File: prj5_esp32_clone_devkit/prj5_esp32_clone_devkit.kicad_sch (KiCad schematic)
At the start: 0 parts

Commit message: Inserimento componenti
Feat: inseriti i simboli dei componenti
Feat: annotati i simboli in modo coerente allo schema di ESP32
Feat: sistemati i posizionamenti
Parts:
- added C1, C21, C3: 22uF/10V(20%), symbol Device:C
- added C14, C22, C9: 0.1uF/50V(10%), symbol Device:C
- added C15: 0.1uF/50V(10%)(NC), symbol Device:C
- added C19: 0.1uf/50V(10%), symbol Device:C
- added C20: 4.7uf/6.3V(10%), symbol Device:C
- added D1: LED, symbol Device:LED
- added D3: D_Schottky, symbol Device:D_Schottky
- added D4, D5, D6: D_TVS, symbol Device:D_TVS
- added J1: USB_B_Micro, symbol Connector:USB_B_Micro
- added J2, J3: Conn_01x19_Pin, symbol Connector:Conn_01x19_Pin
- added MOD1: ESP32-WROOM-32, digikey-footprints:ESP32-WROOM-32D, symbol dk_RF-Transceiver-Modules:ESP32-WROOM-32
- added Q1, Q2: MMSS8050-H-TP, digikey-footprints:SOT-23-3, symbol dk_Transistors-Bipolar-BJT-Single:MMSS8050-H-TP
- added R11, R21, R22: 10K(5%), symbol Device:R
- added R17, R18: 0R(5%), symbol Device:R
- added R2, R24: 2K(5%), symbol Device:R
- added R23: 10K(5%)(NC), symbol Device:R
- added R25: 22.1K(5%), symbol Device:R
- added R28: 47.5K(5%), symbol Device:R
- added SW1, SW2: SW_Push, symbol Switch:SW_Push
- added U1: CP2102N-A01-GQFN28, QFN50P500X500X80-29N, symbol CP2102N-A01-GQFN28:CP2102N-A01-GQFN28
- added U2: AMS1117-3.3, Package_TO_SOT_SMD:SOT-223-3_TabPin2, symbol Regulator_Linear:AMS1117-3.3
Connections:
- new net: U1.29 (GND), U1.3 (GND)
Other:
- note added: "Connector"
- note added: "ESP32 Module"
- note added: "Micro USB 5V & USB-UART"
- note added: "Power Supply"
- note added: "Switch button"

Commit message: Associazione footprint
Feat: associati i footprint ai simboli dello schematico (coerentemente con la BOM)
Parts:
- C1, C21, C3: footprint (none) -> Capacitor_SMD:C_0603_1608Metric
- C14, C15, C19, C20, C22, C9: footprint (none) -> Capacitor_SMD:C_0402_1005Metric
- D1: footprint (none) -> LED_SMD:LED_0603_1608Metric
- D3: footprint (none) -> Diode_SMD:D_SOD-323
- D4, D5, D6: footprint (none) -> Diode_SMD:D_SOD-523
- J1: footprint (none) -> Connector_USB:USB_Micro-AB_Molex_47590-0001
- J2, J3: footprint (none) -> Connector_PinHeader_2.54mm:PinHeader_1x19_P2.54mm_Vertical
- R11, R17, R18, R2, R21, R22, R23, R24, R25, R28: footprint (none) -> Resistor_SMD:R_01005_0402Metric
- SW1, SW2: footprint (none) -> Button_Switch_SMD:SW_SPST_B3S-1000
- U1: footprint QFN50P500X500X80-29N -> Package_DFN_QFN:TQFN-28-1EP_5x5mm_P0.5mm_EP2.7x2.7mm
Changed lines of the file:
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@@
       (effects (font (size 1.27 1.27)))
     )
-    (property "Footprint" "" (at 30.48 98.298 90)
+    (property "Footprint" "Resistor_SMD:R_01005_0402Metric" (at 30.48 98.298 90)
       (effects (font (size 1.27 1.27)) hide)
     )
@@
       (effects (font (size 1.27 1.27)))
     )
-    (property "Footprint" "" (at 38.1 81.788 90)
+    (property "Footprint" "Resistor_SMD:R_01005_0402Metric" (at 38.1 81.788 90)
       (effects (font (size 1.27 1.27)) hide)
     )
@@
       (effects (font (size 1.27 1.27)) (justify left))
     )
-    (property "Footprint" "" (at 144.4752 31.75 0)
+    (property "Footprint" "Capacitor_SMD:C_0402_1005Metric" (at 144.4752 31.75 0)
       (effects (font (size 1.27 1.27)) hide)
     )
@@
       (effects (font (size 1.27 1.27)))
     )
-    (property "Footprint" "" (at 29.21 31.75 0)
+    (property "Footprint" "Connector_USB:USB_Micro-AB_Molex_47590-0001" (at 29.21 31.75 0)
       (effects (font (size 1.27 1.27)) hide)
     )
@@
       (effects (font (size 1.27 1.27)) (justify left))
     )
-    (property "Footprint" "" (at 139.192 46.99 90)
+    (property "Footprint" "Resistor_SMD:R_01005_0402Metric" (at 139.192 46.99 90)
       (effects (font (size 1.27 1.27)) hide)
     )
@@
       (effects (font (size 1.27 1.27)) (justify left))
     )
-    (property "Footprint" "" (at 28.702 153.67 90)
+    (property "Footprint" "Resistor_SMD:R_01005_0402Metric" (at 28.702 153.67 90)
       (effects (font (size 1.27 1.27)) hide)
     )
@@
       (effects (font (size 1.27 1.27)) (justify right))
     )
-    (property "Footprint" "" (at 30.48 165.1 0)
+    (property "Footprint" "LED_SMD:LED_0603_1608Metric" (at 30.48 165.1 0)
       (effects (font (size 1.27 1.27)) hide)
     )
@@
       (effects (font (size 1.27 1.27)) (justify left))
     )
-    (property "Footprint" "" (at 189.992 54.61 90)
+    (property "Footprint" "Resistor_SMD:R_01005_0402Metric" (at 189.992 54.61 90)
       (effects (font (size 1.27 1.27)) hide)
     )
@@
       (effects (font (size 1.27 1.27)) (justify left))
     )
-    (property "Footprint" "" (at 45.4152 162.56 0)
+    (property "Footprint" "Capacitor_SMD:C_0603_1608Metric" (at 45.4152 162.56 0)
       (effects (font (size 1.27 1.27)) hide)
     )
@@
       (effects (font (size 1.27 1.27)))
     )
-    (property "Footprint" "" (at 29.21 113.538 90)
+    (property "Footprint" "Resistor_SMD:R_01005_0402Metric" (at 29.21 113.538 90)
       (effects (font (size 1.27 1.27)) hide)
     )
@@
       (effects (font (size 1.27 1.27)))
     )
-    (property "Footprint" "" (at 73.66 76.708 90)
+    (property "Footprint" "Resistor_SMD:R_01005_0402Metric" (at 73.66 76.708 90)
       (effects (font (size 1.27 1.27)) hide)
     )
@@
       (effects (font (size 1.27 1.27)) (justify left))
     )
-    (property "Footprint" "" (at 192.7352 40.64 0)
+    (property "Footprint" "Capacitor_SMD:C_0603_1608Metric" (at 192.7352 40.64 0)
       (effects (font (size 1.27 1.27)) hide)
     )
@@
       (effects (font (size 1.27 1.27)) (justify left))
     )
-    (property "Footprint" "" (at 192.7352 71.12 0)
+    (property "Footprint" "Capacitor_SMD:C_0402_1005Metric" (at 192.7352 71.12 0)
       (effects (font (size 1.27 1.27)) hide)
     )
@@
       (effects (font (size 1.27 1.27)) (justify right))
     )
-    (property "Footprint" "" (at 58.42 39.37 0)
+    (property "Footprint" "Diode_SMD:D_SOD-523" (at 58.42 39.37 0)
       (effects (font (size 1.27 1.27)) hide)
     )
@@
       (effects (font (size 1.27 1.27)))
     )
-    (property "Footprint" "" (at 38.1 71.628 90)
+    (property "Footprint" "Resistor_SMD:R_01005_0402Metric" (at 38.1 71.628 90)
       (effects (font (size 1.27 1.27)) hide)
     )
@@
       (effects (font (size 1.27 1.27)))
     )
-    (property "Footprint" "" (at 147.32 40.513 90)
+    (property "Footprint" "Resistor_SMD:R_01005_0402Metric" (at 147.32 40.513 90)
       (effects (font (size 1.27 1.27)) hide)
     )
@@
       (effects (font (size 1.27 1.27)))
     )
-    (property "Footprint" "" (at 227.33 132.08 0)
+    (property "Footprint" "Connector_PinHeader_2.54mm:PinHeader_1x19_P2.54mm_Vertical" (at 227.33 132.08 0)
       (effects (font (size 1.27 1.27)) hide)
     )
@@
       (effects (font (size 1.27 1.27)) (justify right))
     )
-    (property "Footprint" "" (at 38.1 39.37 0)
+    (property "Footprint" "Diode_SMD:D_SOD-523" (at 38.1 39.37 0)
       (effects (font (size 1.27 1.27)) hide)
     )
@@
       (effects (font (size 1.27 1.27)) (justify left))
     )
-    (property "Footprint" "" (at 78.4352 162.56 0)
+    (property "Footprint" "Capacitor_SMD:C_0603_1608Metric" (at 78.4352 162.56 0)
       (effects (font (size 1.27 1.27)) hide)
     )
@@
       (effects (font (size 1.27 1.27)))
     )
-    (property "Footprint" "" (at 265.43 132.08 0)
+    (property "Footprint" "Connector_PinHeader_2.54mm:PinHeader_1x19_P2.54mm_Vertical" (at 265.43 132.08 0)
       (effects (font (size 1.27 1.27)) hide)
     )
@@
       (effects (font (size 1.27 1.27)) (justify right))
     )
-    (property "Footprint" "" (at 48.26 39.37 0)
+    (property "Footprint" "Diode_SMD:D_SOD-523" (at 48.26 39.37 0)
       (effects (font (size 1.27 1.27)) hide)
     )
@@
       (effects (font (size 1.27 1.27)) (justify left))
     )
-    (property "Footprint" "" (at 209.2452 40.64 0)
+    (property "Footprint" "Capacitor_SMD:C_0402_1005Metric" (at 209.2452 40.64 0)
       (effects (font (size 1.27 1.27)) hide)
     )
@@
       (effects (font (size 1.27 1.27)))
     )
-    (property "Footprint" "QFN50P500X500X80-29N" (at 106.68 64.77 0)
+    (property "Footprint" "Package_DFN_QFN:TQFN-28-1EP_5x5mm_P0.5mm_EP2.7x2.7mm" (at 106.68 64.77 0)
       (effects (font (size 1.27 1.27)) (justify bottom) hide)
     )
@@
       (effects (font (size 1.27 1.27)))
     )
-    (property "Footprint" "" (at 128.27 164.1348 0)
+    (property "Footprint" "Capacitor_SMD:C_0402_1005Metric" (at 128.27 164.1348 0)
       (effects (font (size 1.27 1.27)) hide)
     )
@@
       (effects (font (size 1.27 1.27)))
     )
-    (property "Footprint" "" (at 152.4 147.32 0)
+    (property "Footprint" "Button_Switch_SMD:SW_SPST_B3S-1000" (at 152.4 147.32 0)
       (effects (font (size 1.27 1.27)) hide)
     )
@@
       (effects (font (size 1.27 1.27)))
     )
-    (property "Footprint" "" (at 156.21 164.1348 0)
+    (property "Footprint" "Capacitor_SMD:C_0402_1005Metric" (at 156.21 164.1348 0)
       (effects (font (size 1.27 1.27)) hide)
     )
@@
       (effects (font (size 1.27 1.27)) (justify left))
     )
-    (property "Footprint" "" (at 149.352 78.74 90)
+    (property "Footprint" "Resistor_SMD:R_01005_0402Metric" (at 149.352 78.74 90)
       (effects (font (size 1.27 1.27)) hide)
     )
@@
       (effects (font (size 1.27 1.27)) (justify left))
     )
-    (property "Footprint" "" (at 158.4452 31.75 0)
+    (property "Footprint" "Capacitor_SMD:C_0402_1005Metric" (at 158.4452 31.75 0)
       (effects (font (size 1.27 1.27)) hide)
     )
@@
       (effects (font (size 1.27 1.27)))
     )
-    (property "Footprint" "" (at 64.77 25.4 0)
+    (property "Footprint" "Diode_SMD:D_SOD-323" (at 64.77 25.4 0)
       (effects (font (size 1.27 1.27)) hide)
     )
@@
       (effects (font (size 1.27 1.27)))
     )
-    (property "Footprint" "" (at 124.46 147.32 0)
-      (effects (font (size 1.27 1.27)) hide)
-    )
+    (property "Footprint" "Button_Switch_SMD:SW_SPST_B3S-1000" (at 124.46 147.32 0)
+      (effects (font (size 1.27 1.27)) hide)
+    )

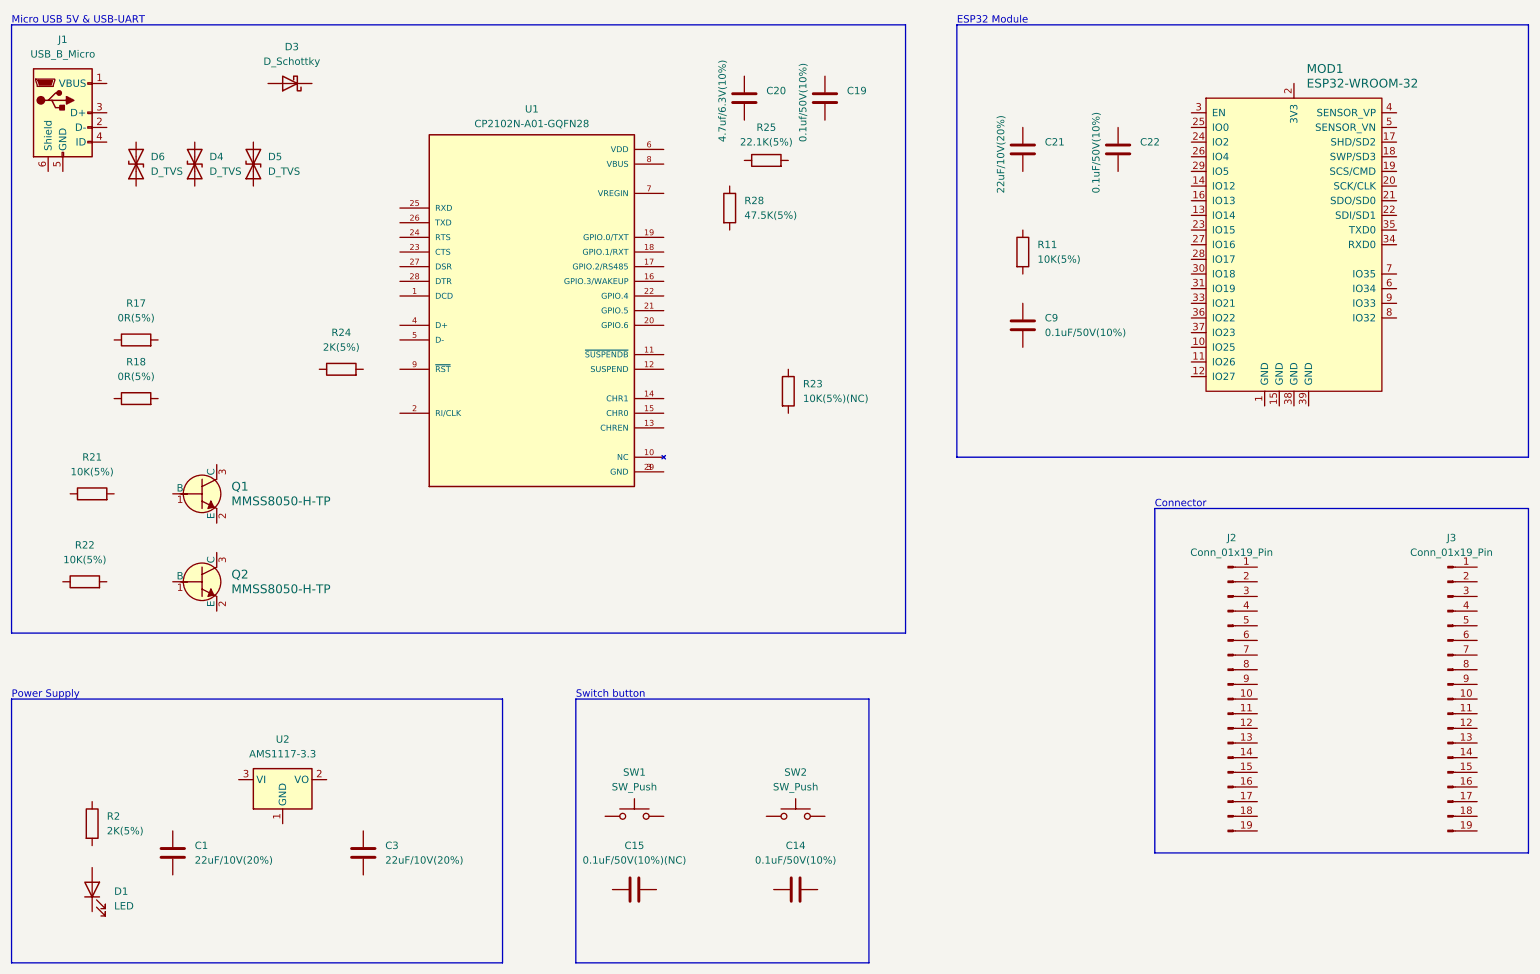
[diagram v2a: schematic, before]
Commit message: Connessioni componenti schematico
Feat: concluso il wiring dei simboli
Feat: aggiustati alcuni posizionamenti
Feat: aggiunto commento con tabella di verità
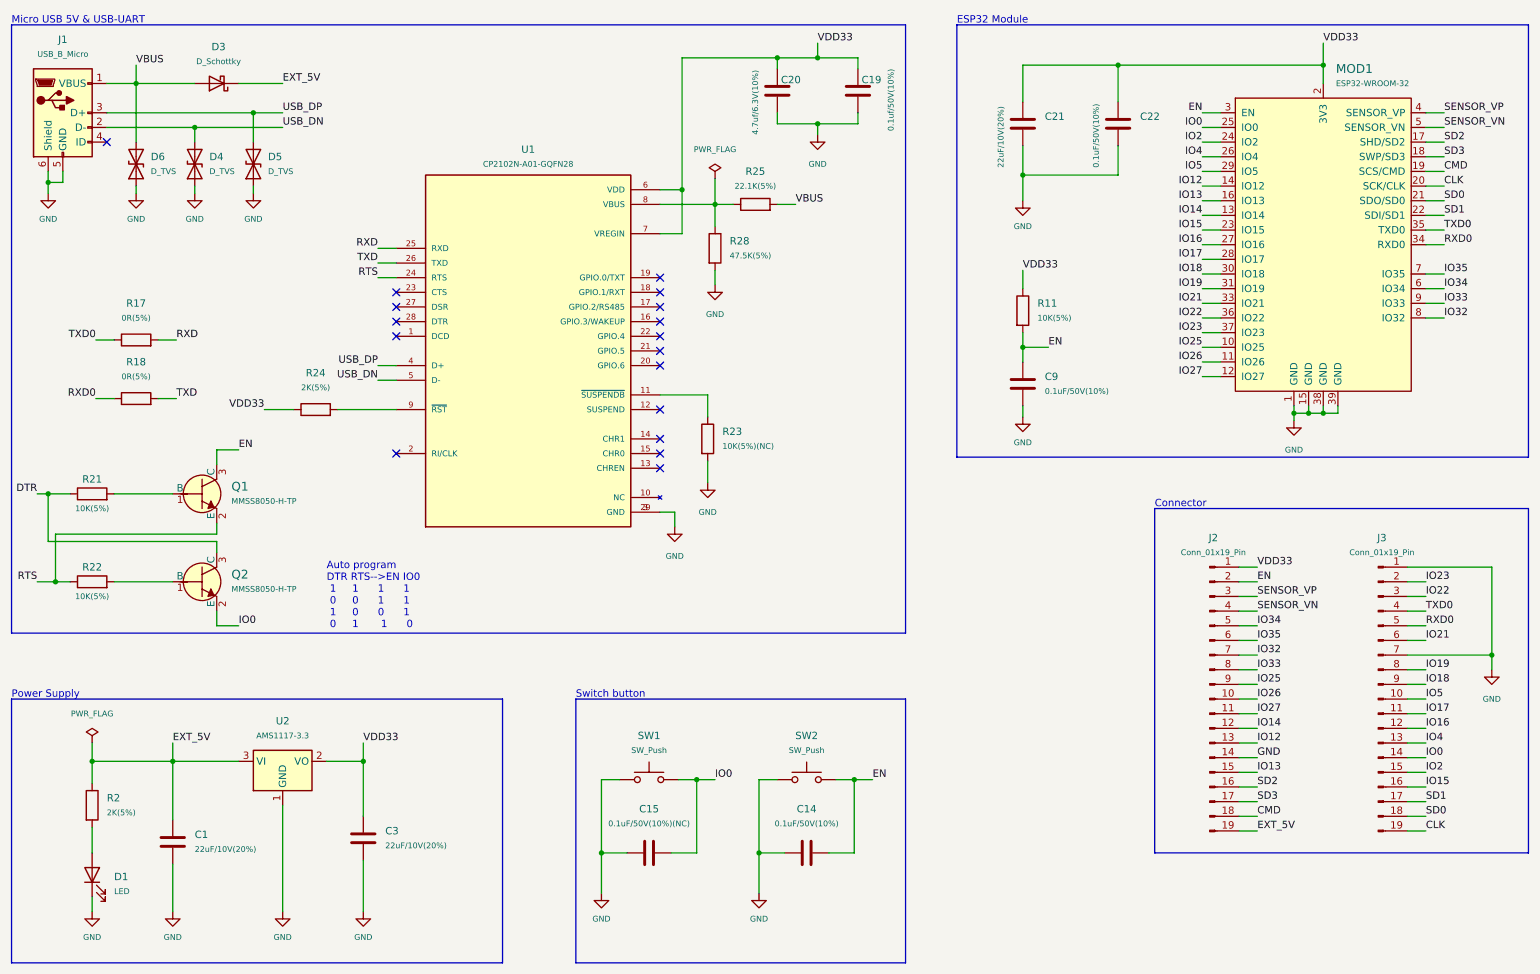
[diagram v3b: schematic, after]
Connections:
- net DTR: now reaches R21.1
- net DTR: now also Q2.3 (C)
- net at R21.2: now also Q1.1 (B)
- net RXD0: now reaches R18.1
- net RXD0: now also J3.5 (Pin_5), MOD1.34 (RXD0)
- net TXD: now reaches R18.2
- net TXD: now also U1.26 (TXD)
- net VDD33: now reaches C20.1
- net VDD33: now also C19.1, C21.1, C22.1, C3.1, J2.1 (Pin_1), MOD1.2 (3V3), R11.1, R24.1, U1.6 (VDD), U1.7 (VREGIN), U2.2 (VO)
- net GND: now reaches C20.2
- net GND: now also C1.2, C14.1, C15.1, C19.2, C21.2, C22.2, C3.2, C9.2, D1.1 (K), D4.1 (A1), D5.1 (A1), D6.1 (A1), J1.5 (GND), J1.6 (Shield), J2.14 (Pin_14), J3.1 (Pin_1), J3.7 (Pin_7), MOD1.1 (GND), MOD1.15 (GND), MOD1.38 (GND), MOD1.39 (GND), R23.2, R28.2, SW1.1, SW2.1, U1.29 (GND), U1.3 (GND), U2.1 (GND)
- net VBUS: now reaches J1.1 (VBUS)
- net VBUS: now also D3.2 (A), D6.2 (A2), R25.2
- net USB_DN: now reaches J1.2 (D-)
- net USB_DN: now also D4.2 (A2), U1.5 (D-)
- net USB_DP: now reaches J1.3 (D+)
- net USB_DP: now also D5.2 (A2), U1.4 (D+)
- net at R28.1: now also R25.1, U1.8 (VBUS)
- net EXT_5V: now reaches R2.1
- net EXT_5V: now also C1.1, D3.1 (K), J2.19 (Pin_19), U2.3 (VI)
- net at R2.2: now also D1.2 (A)
- net EN: now reaches R11.2
- net EN: now also C14.2, C9.1, J2.2 (Pin_2), MOD1.3 (EN), Q1.3 (C), SW2.2
- net RTS: now reaches R22.1
- net RTS: now also Q1.2 (E), U1.24 (RTS)
- net at R22.2: now also Q2.1 (B)
- net at R24.2: now also U1.9 (~{RST})
- net TXD0: now reaches R17.1
- net TXD0: now also J3.4 (Pin_4), MOD1.35 (TXD0)
- net RXD: now reaches R17.2
- net RXD: now also U1.25 (RXD)
- net IO26: now reaches J2.10 (Pin_10)
- net IO26: now also MOD1.11 (IO26)
- net IO27: now reaches J2.11 (Pin_11)
- net IO27: now also MOD1.12 (IO27)
- net IO14: now reaches J2.12 (Pin_12)
- net IO14: now also MOD1.13 (IO14)
- net IO12: now reaches J2.13 (Pin_13)
- net IO12: now also MOD1.14 (IO12)
- net IO13: now reaches J2.15 (Pin_15)
- net IO13: now also MOD1.16 (IO13)
- net SD2: now reaches J2.16 (Pin_16)
- net SD2: now also MOD1.17 (SHD/SD2)
- net SD3: now reaches J2.17 (Pin_17)
- net SD3: now also MOD1.18 (SWP/SD3)
- net CMD: now reaches J2.18 (Pin_18)
- net CMD: now also MOD1.19 (SCS/CMD)
- net SENSOR_VP: now reaches J2.3 (Pin_3)
- net SENSOR_VP: now also MOD1.4 (SENSOR_VP)
- net SENSOR_VN: now reaches J2.4 (Pin_4)
- net SENSOR_VN: now also MOD1.5 (SENSOR_VN)
- net IO34: now reaches J2.5 (Pin_5)
- net IO34: now also MOD1.6 (IO34)
- net IO35: now reaches J2.6 (Pin_6)
- net IO35: now also MOD1.7 (IO35)
- net IO32: now reaches J2.7 (Pin_7)
- net IO32: now also MOD1.8 (IO32)
- net IO33: now reaches J2.8 (Pin_8)
- net IO33: now also MOD1.9 (IO33)
- net IO25: now reaches J2.9 (Pin_9)
- net IO25: now also MOD1.10 (IO25)
- net IO5: now reaches J3.10 (Pin_10)
- net IO5: now also MOD1.29 (IO5)
- net IO17: now reaches J3.11 (Pin_11)
- net IO17: now also MOD1.28 (IO17)
- net IO16: now reaches J3.12 (Pin_12)
- net IO16: now also MOD1.27 (IO16)
- net IO4: now reaches J3.13 (Pin_13)
- net IO4: now also MOD1.26 (IO4)
- net IO0: now reaches J3.14 (Pin_14)
- net IO0: now also C15.2, MOD1.25 (IO0), Q2.2 (E), SW1.2
- net IO2: now reaches J3.15 (Pin_15)
- net IO2: now also MOD1.24 (IO2)
- net IO15: now reaches J3.16 (Pin_16)
- net IO15: now also MOD1.23 (IO15)
- net SD1: now reaches J3.17 (Pin_17)
- net SD1: now also MOD1.22 (SDI/SD1)
- net SD0: now reaches J3.18 (Pin_18)
- net SD0: now also MOD1.21 (SDO/SD0)
- net CLK: now reaches J3.19 (Pin_19)
- net CLK: now also MOD1.20 (SCK/CLK)
- net IO23: now reaches J3.2 (Pin_2)
- net IO23: now also MOD1.37 (IO23)
- net IO22: now reaches J3.3 (Pin_3)
- net IO22: now also MOD1.36 (IO22)
- net IO21: now reaches J3.6 (Pin_6)
- net IO21: now also MOD1.33 (IO21)
- net IO19: now reaches J3.8 (Pin_8)
- net IO19: now also MOD1.31 (IO19)
- net IO18: now reaches J3.9 (Pin_9)
- net IO18: now also MOD1.30 (IO18)
- net at U1.11 (~{SUSPENDB}): now also R23.1
- no-connect marks 0 -> 17
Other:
- note added: "Auto program DTR RTS-->EN IO0 1 1 1 1 0 0 1 1 1 0 0 1 0 1 1 0"
- moved on the sheet: C1, C14, C15, C19, C20, C21, C22, C3, C9, D1, D3, J2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

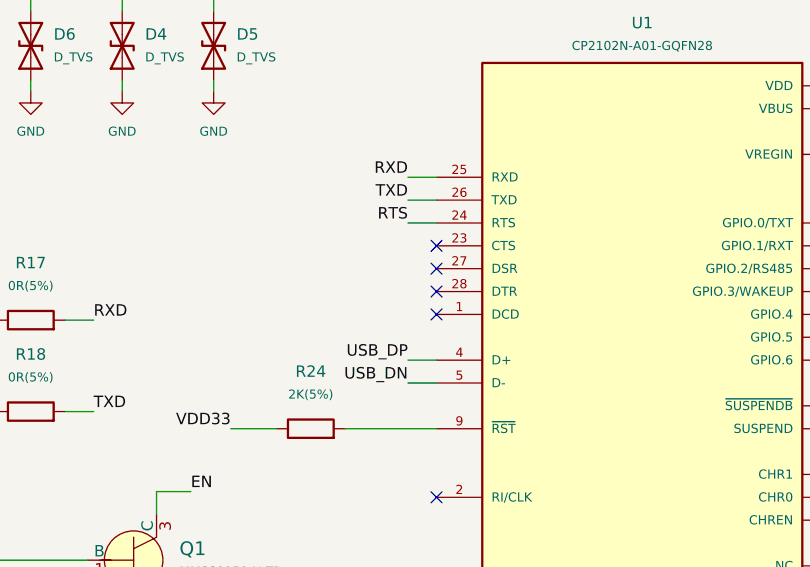
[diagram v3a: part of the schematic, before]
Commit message: Connessioni footprint e fix
Feat: create gran parte delle connessioni su Pcbnew
Fix: sistemato il track width della classe POWER
Fix: sistemata connessione nello schematico, mancava label DTR su pin 28 di U1
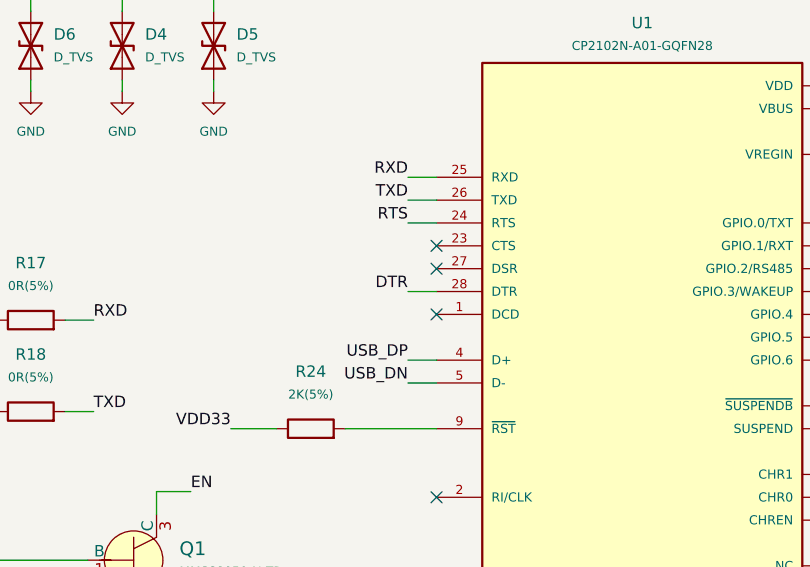
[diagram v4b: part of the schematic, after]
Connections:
- net DTR: now also U1.28 (DTR)
- no-connect marks 17 -> 16
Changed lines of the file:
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@@
   (no_connect (at 83.185 61.595))
   (no_connect (at 128.905 74.295))
-  (no_connect (at 83.185 66.675))
   (wire (pts (xy 138.43 46.355) (xy 141.605 46.355))
     (stroke (width 0) (type default))
@@
   )
   (wire (pts (xy 222.885 71.12) (xy 226.06 71.12))
+    (stroke (width 0) (type default))
+  )
+  (wire (pts (xy 80.01 66.675) (xy 83.185 66.675))
     (stroke (width 0) (type default))
   )
@@
     (effects (font (size 1.27 1.27)) (justify left bottom))
   )
+  (label "DTR" (at 80.01 66.675 180) (fields_autoplaced)
+    (effects (font (size 1.27 1.27)) (justify right bottom))
+  )
   (label "EXT_5V" (at 63.5 25.4 0) (fields_autoplaced)
